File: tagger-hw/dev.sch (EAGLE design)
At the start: 7 parts, among them IC1 4050D, IC2 LP298XS, X1 MICROSD

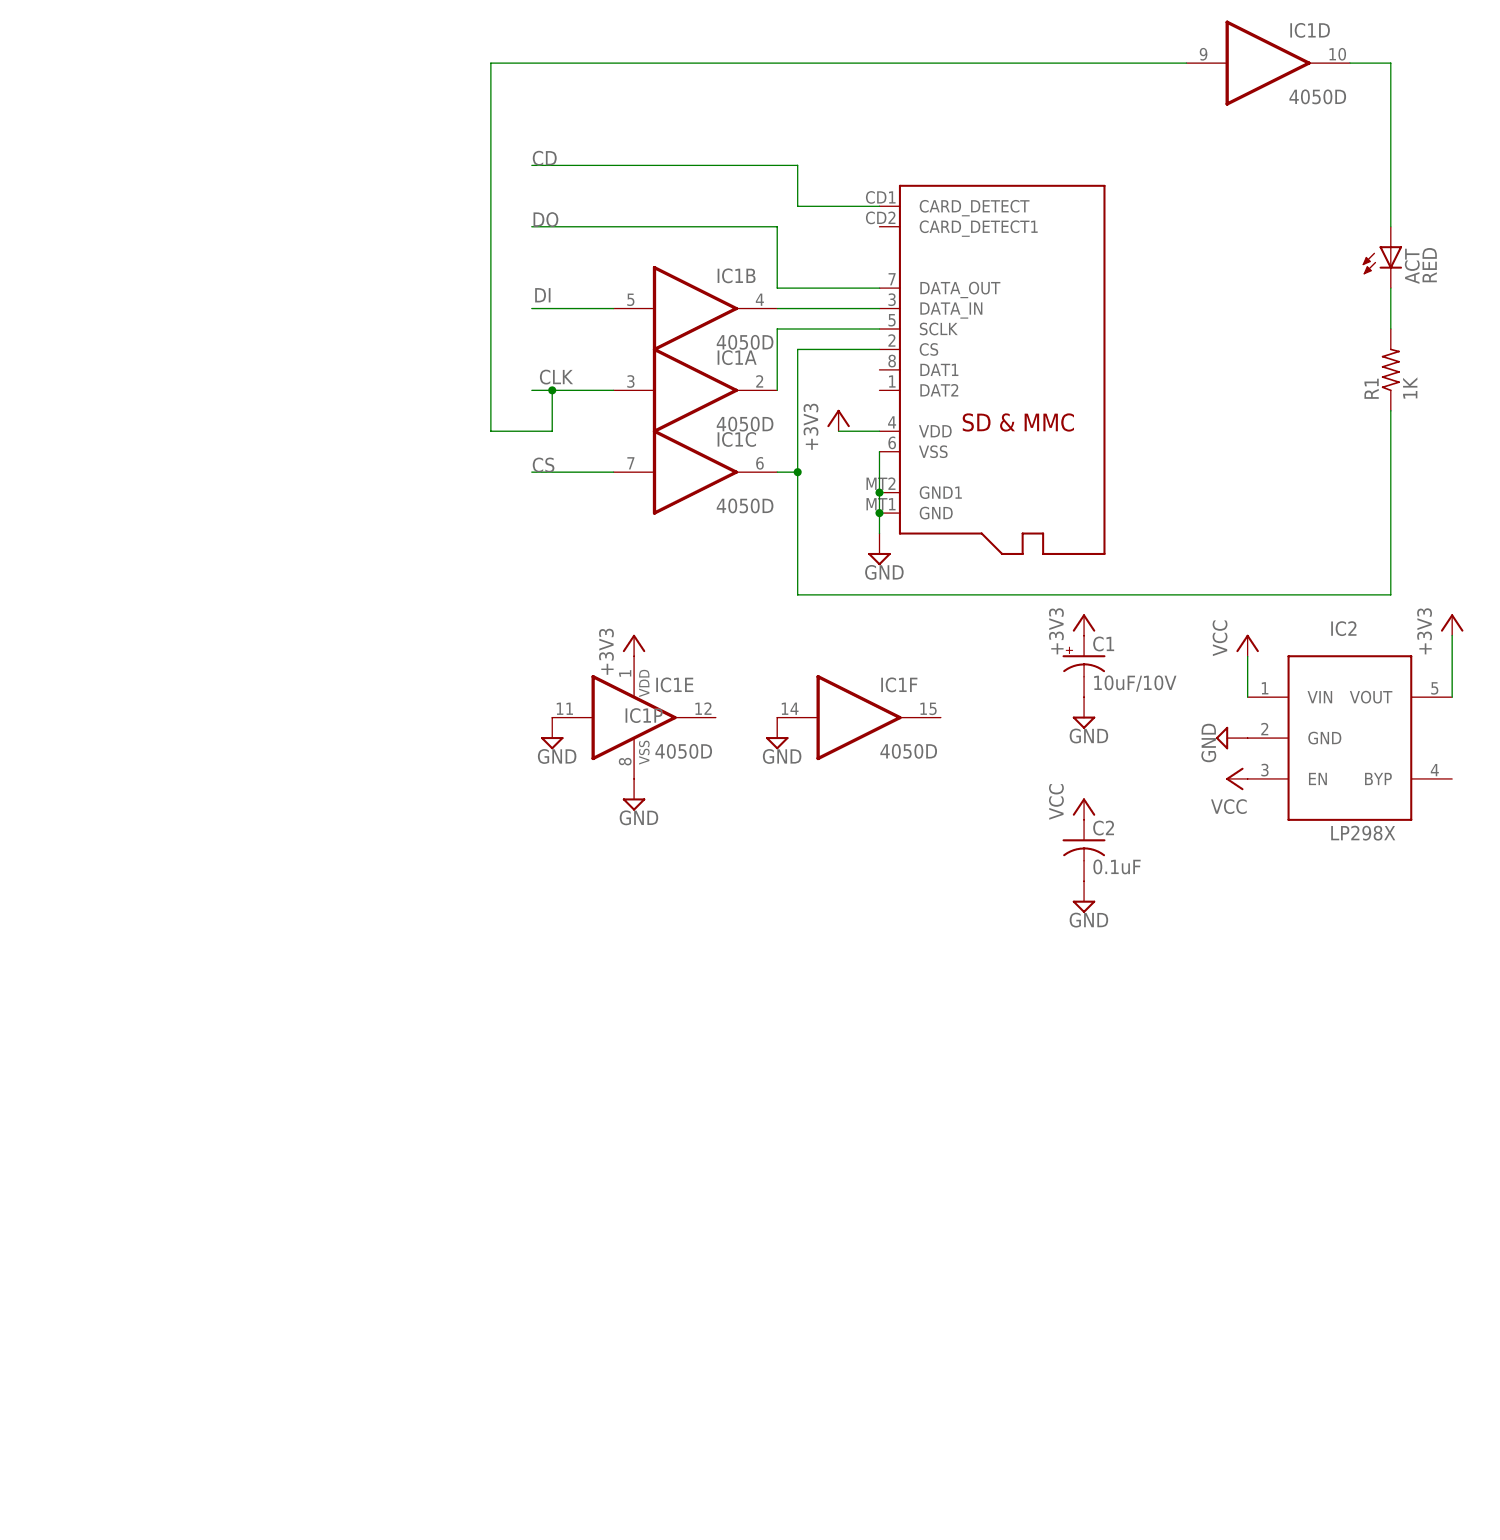
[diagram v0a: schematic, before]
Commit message: Add Arduino example, rename main to dev
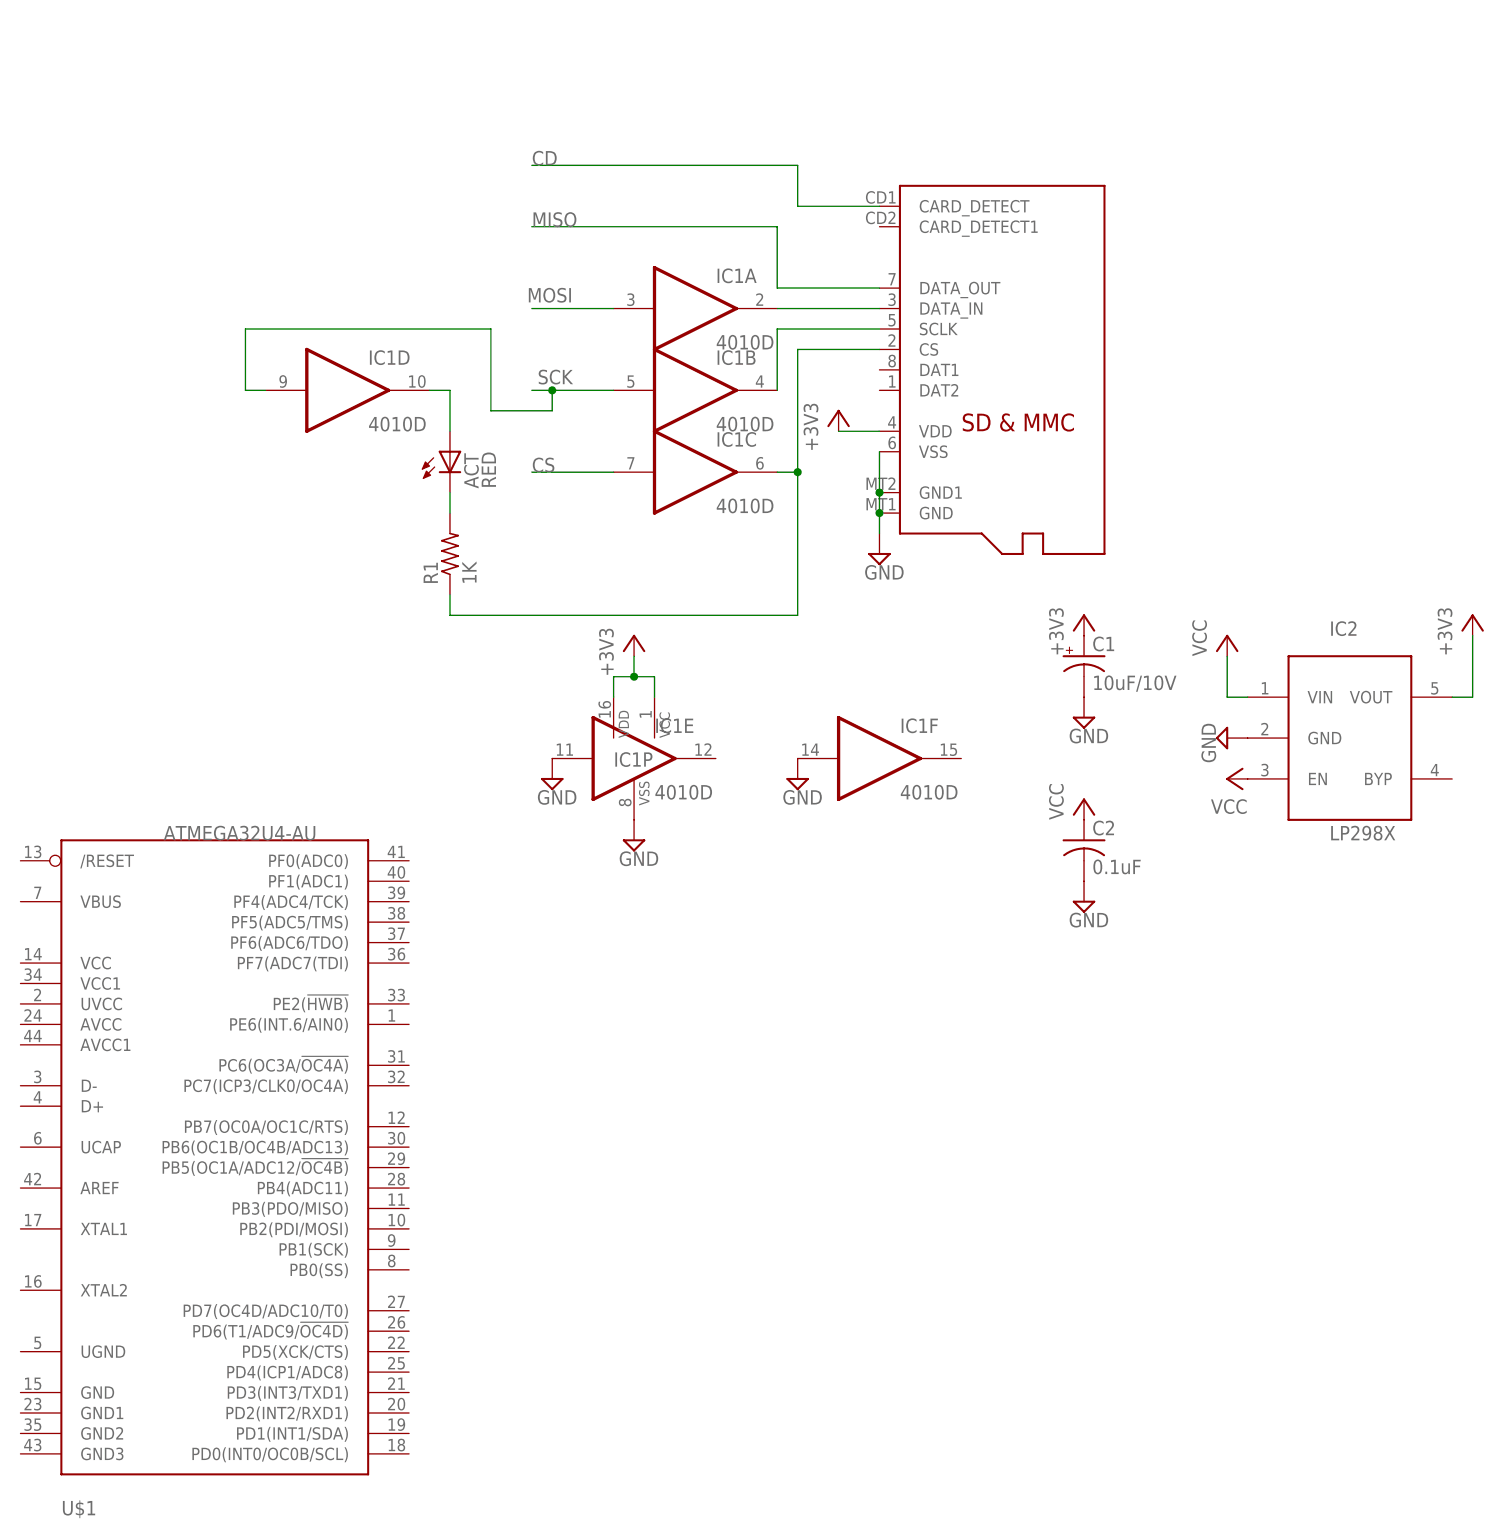
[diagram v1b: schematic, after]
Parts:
- added U$1: ATMEGA32U4-AU, adafruit:ATMEGA32U4-AU
- IC1: value 4050D -> 4010D; device 40xx:4050D -> 40xx:4010D
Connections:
- net DO renamed MISO
- removed net CLK: IC1A.I, IC1D.I
- removed net DI: IC1B.I
- new net MOSI: IC1A.I
- new net SCK: IC1B.I, IC1D.I
- net +3V3: now also IC1P.VCC
- net N$2: now also IC1B.O; no longer IC1A.O
- net N$5: now also IC1A.O; no longer IC1B.O
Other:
- moved on the sheet: ACT, IC1A, IC1B, IC1D, IC1E, IC1F, R1

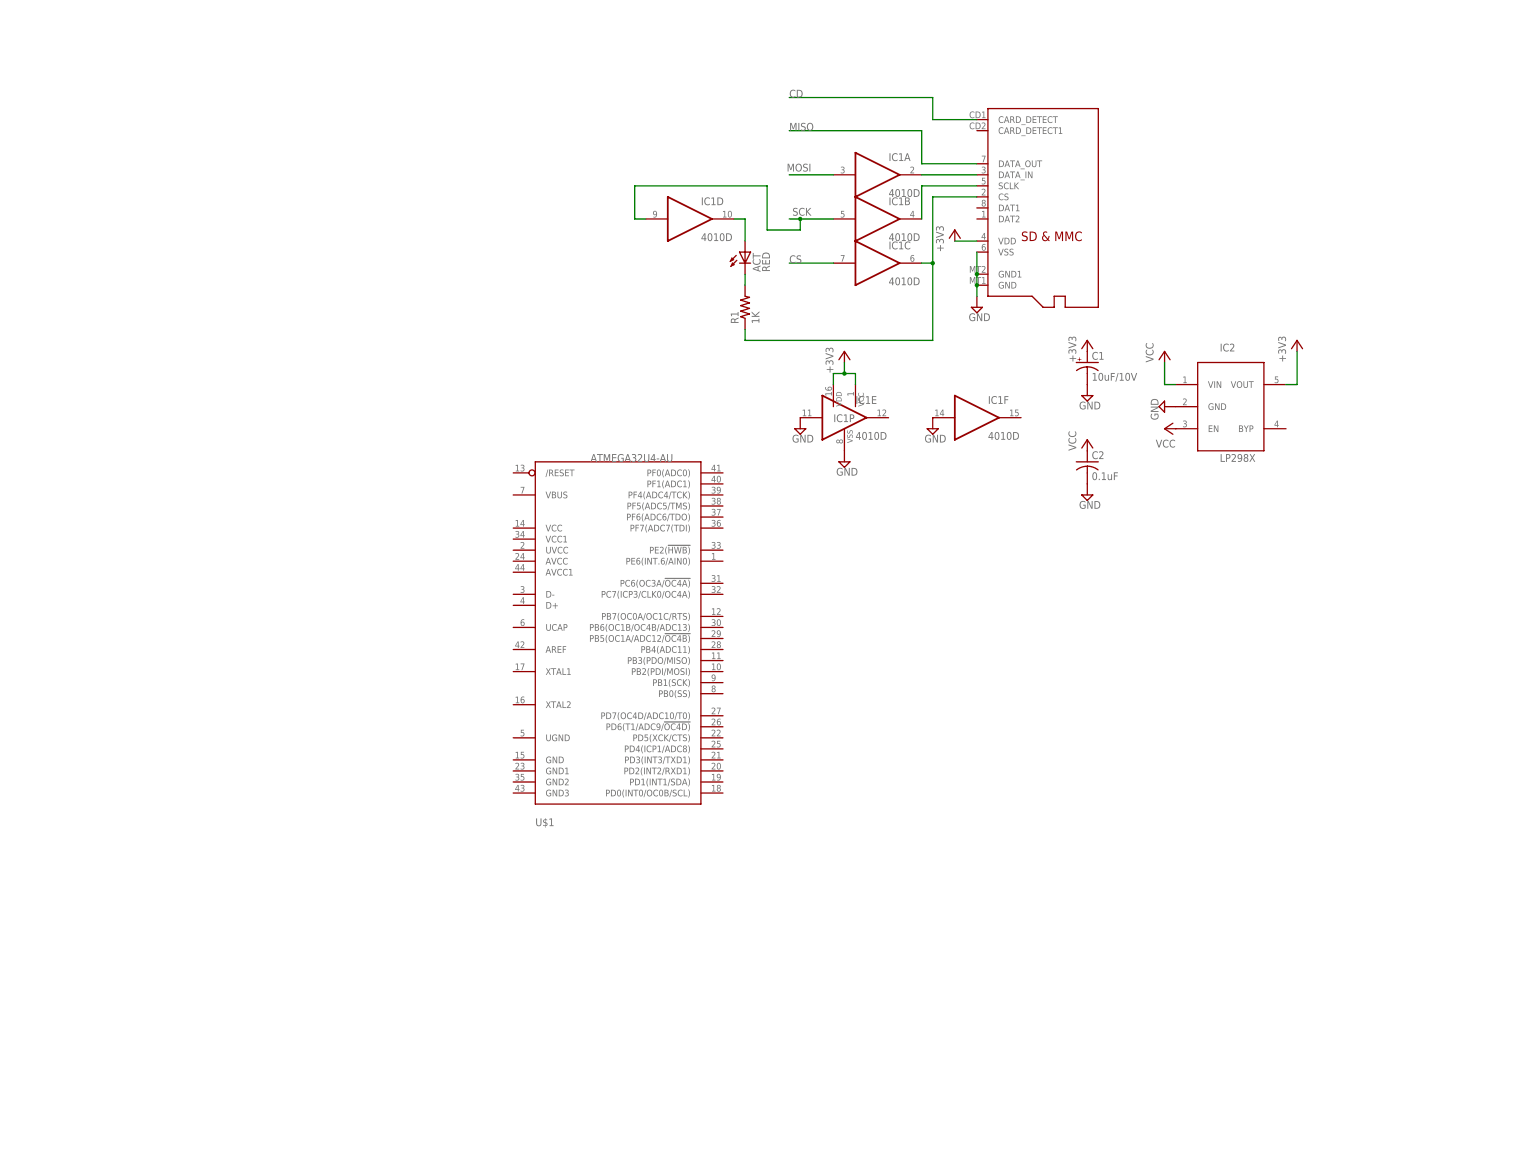
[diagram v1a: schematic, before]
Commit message: Placement/layout done except for SPI RTC
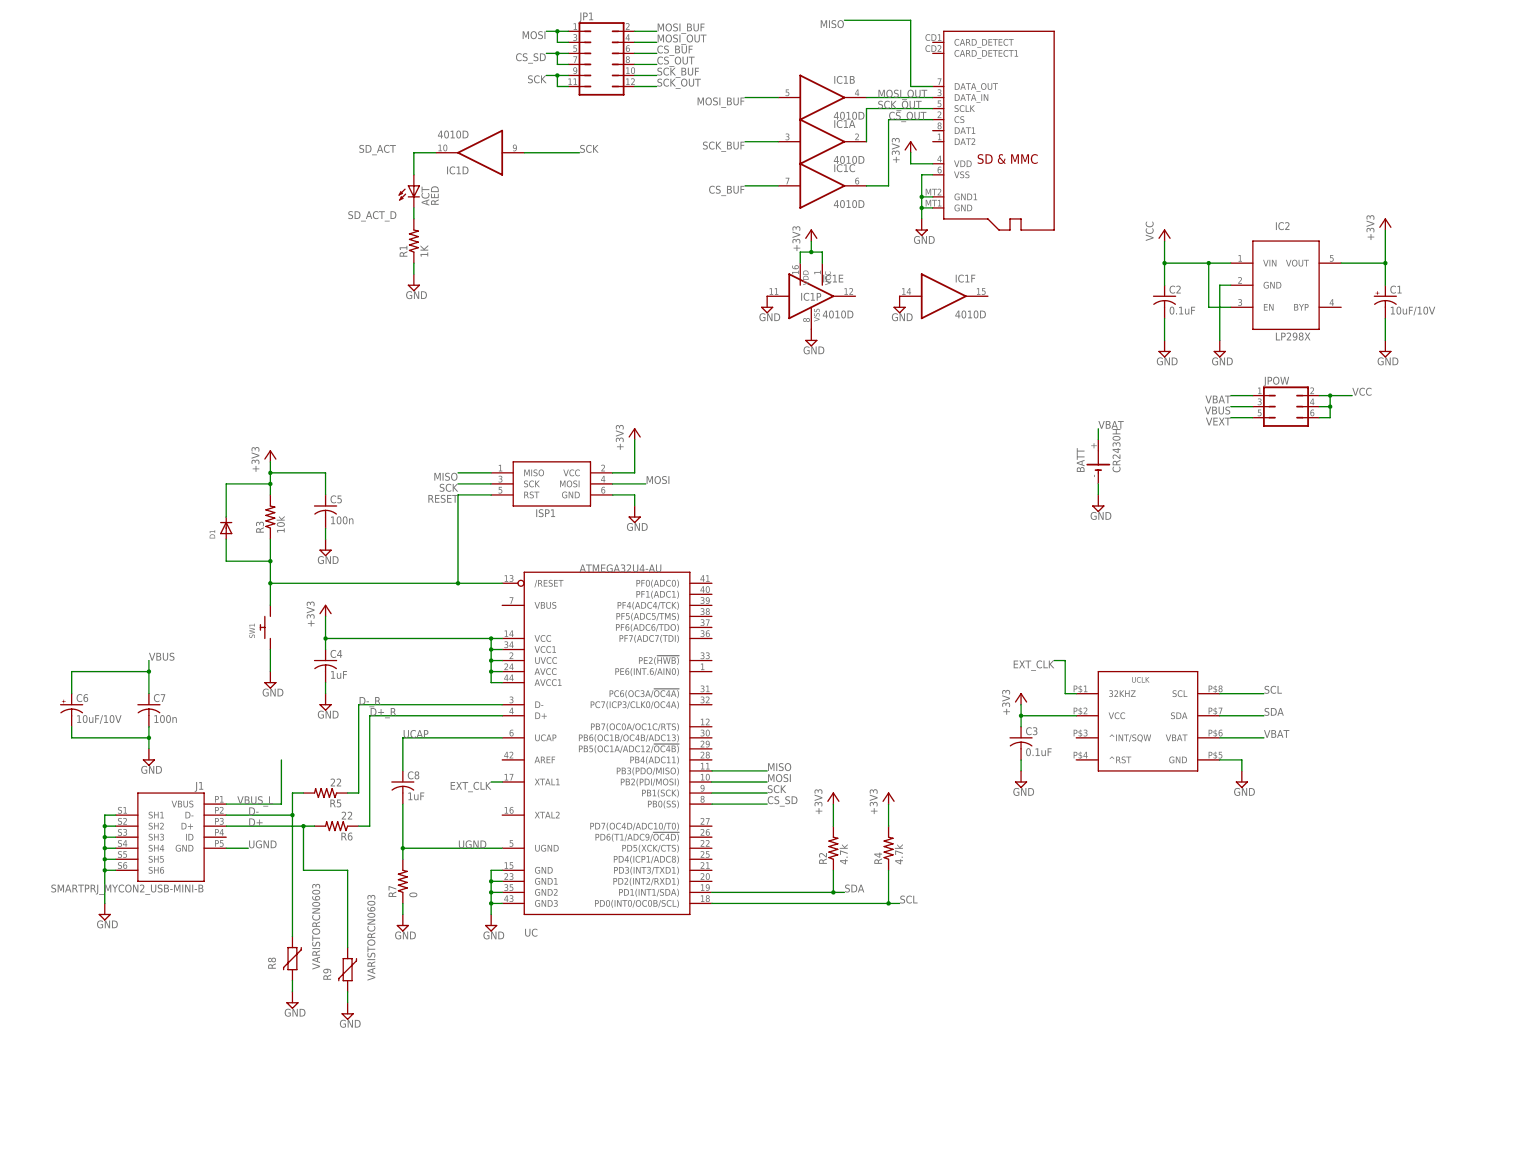
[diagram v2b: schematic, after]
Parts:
- removed U$1: ATMEGA32U4-AU, adafruit:ATMEGA32U4-AU
- added BATT: CR2430H, battery:CR2430H
- added C3: 0.1uF, adafruit:C-USC0805K
- added C4, C8: 1uF, rcl:C-USC0603
- added C5, C7: 100n, rcl:C-USC0603
- added C6: 10uF/10V, adafruit:CPOL-USA/3216-18R
- added D1: (no value), adafruit:DIODESOD-123
- added ISP1: AVRISP-6, adafruit:AVRISP-6
- added J1: SMARTPRJ_MYCON2_USB-MINI-B, dorskyee:SMARTPRJ_MYCON2_USB-MINI-B
- added JP1: (no value), jumper:JP6Q
- added JPOW: (no value), jumper:JP3Q
- added R2, R4: 4.7k, resistor:R-US_R0603
- added R3: 10k, resistor:R-US_R0603
- added R5, R6: 22, resistor:R-US_R0603
- added R7: 0, resistor:R-US_R0603
- added R8, R9: VARISTORCN0603, varistor:VARISTORCN0603
- added SW1: (no value), adafruit:SWITCH_PUSHBUTTONSOFTTOUCHSMD_SJ
- added UC: ATMEGA32U4-AU, adafruit:ATMEGA32U4-AU
- added UCLK: DS3231MDS3231MZ+, dorskyee:DS3231MDS3231MZ+
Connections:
- net N$1 renamed SD_ACT
- net N$4 renamed SD_ACT_D
- removed net CD: X1.CARD_DETECT
- removed net CS: IC1C.I
- removed net N$2: IC1B.O, X1.SCLK
- removed net N$3: IC1C.O, R1.1, X1.CS
- removed net N$5: IC1A.O, X1.DATA_IN
- new net CS_BUF: IC1C.I, JP1.6
- new net CS_OUT: IC1C.O, JP1.8, X1.CS
- new net CS_SD: JP1.5, JP1.7, UC.PB0(SS)
- new net D+: J1.D+, R6.2, R9.1
- new net D+_R: R6.1, UC.D+
- new net D-: J1.D-, R5.2, R8.1
- new net D-_R: R5.1, UC.D-
- new net EXT_CLK: UC.XTAL1, UCLK.32KHZ
- new net MOSI_BUF: IC1B.I, JP1.2
- new net MOSI_OUT: IC1B.O, JP1.4, X1.DATA_IN
- new net RESET: D1.A, ISP1.RST, R3.1, SW1.P$2, UC./RESET
- new net SCK_BUF: IC1A.I, JP1.10
- new net SCK_OUT: IC1A.O, JP1.12, X1.SCLK
- new net SCL: R4.1, UC.PD0(INT0/OC0B/SCL), UCLK.SCL
- new net SDA: R2.1, UC.PD1(INT1/SDA), UCLK.SDA
- new net UCAP: C8.1, UC.UCAP
- new net UGND: C8.2, J1.GND, R7.2, UC.UGND
- new net VBAT: BATT.+, JPOW.1, UCLK.VBAT
- new net VBUS: C6.+, C7.1, JPOW.3
- new net VBUS_L: J1.VBUS
- new net VEXT: JPOW.5
- net +3V3: now also C3.1, C4.1, C5.1, D1.C, ISP1.VCC, R2.2, R3.2, R4.2, UC.AVCC, UC.AVCC1, UC.UVCC, UC.VCC, UC.VCC1, UCLK.VCC
- net GND: now also BATT.-, C3.2, C4.2, C5.2, C6.-, C7.2, ISP1.GND, J1.SH1, J1.SH2, J1.SH3, J1.SH4, J1.SH5, J1.SH6, R1.1, R7.1, R8.2, R9.2, SW1.P$1, UC.GND, UC.GND1, UC.GND2, UC.GND3, UCLK.GND
- net MISO: now also ISP1.MISO, UC.PB3(PDO/MISO)
- net MOSI: now also ISP1.MOSI, JP1.1, JP1.3, UC.PB2(PDI/MOSI); no longer IC1A.I
- net SCK: now also ISP1.SCK, JP1.11, JP1.9, UC.PB1(SCK); no longer IC1B.I
- net VCC: now also JPOW.2, JPOW.4, JPOW.6
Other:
- moved on the sheet: ACT, C1, C2, IC1A, IC1B, IC1C, IC1D, IC1E, IC1F, IC1P, IC2, R1

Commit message: dev_v0 routing/placement lock
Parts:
- removed SW1: (no value), adafruit:SWITCH_PUSHBUTTONSOFTTOUCHSMD_SJ
- added C9: 0.1uF, adafruit:C-USC0805K
- added F1: MF-MSMF050-2, adafruit:PTCFUSE-1812
- added R10: 1k, resistor:R-US_R0603
- added R11: 100k, resistor:R-US_R0603
- added S1: B3F-1002, switch-omron:10-XX
- added SV1: SSA-132-S-T, con-lsta:FE05-1
- added U$1: EXC-31B, dorskyee:EXC-31B
- added U$2: MH2029-300Y, dorskyee:MH2029-300Y
- added UCLK2: DS1347T+, dorskyee:DS1347T+
- added X2, X3: 22-23-2021, con-molex:22-23-2021
- D1: value (none) -> 1N4148W-7-F
- JP1, JPOW: value (none) -> HDR100IMP40M-G-V-TH
- renumbered UCLK to UCLK1
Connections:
- removed net VBUS_L: J1.VBUS
- new net CS_RTC: UC.PB4(ADC11), UCLK2.SCLK
- new net PPS: SV1.1, UC.PB6(OC1B/OC4B/ADC13)
- new net RTC_X1: U$1.2, UCLK2.X1
- new net RTC_X2: U$1.1, UCLK2.X2
- new net RX: SV1.2, UC.PD2(INT2/RXD1)
- new net TRIG_H: R10.1, X2-1.S
- new net TRIG_L: R11.2, UC.PB5(OC1A/ADC12/!OC4B), X2-2.S
- new net TX: SV1.3, UC.PD3(INT3/TXD1)
- new net VBUS_F: F1.1, J1.VBUS
- net +3V3: now also C9.1, R10.2, SV1.5, UCLK2.VCC
- net GND: now also C9.2, R11.1, S1.P, S1.P1, SV1.4, U$2.1, UCLK2.GND, X3-2.S; no longer SW1.P$1
- net MISO: now also UCLK2.DOUT
- net MOSI: now also UCLK2.DIN
- net RESET: now also S1.S, S1.S1; no longer SW1.P$2
- net UGND: now also U$2.2
- net VBUS: now also F1.2, UC.VBUS
- net VEXT: now also X3-1.S
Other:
- moved on the sheet: BATT, JP1, JPOW
